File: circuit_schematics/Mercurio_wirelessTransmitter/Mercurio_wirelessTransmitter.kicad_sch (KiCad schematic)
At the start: 61 parts, among them J1 USB_B, J2 SIM_CARD_SLOT, J3 MAIN_ANTENNA, J4 SENSOR_IN, J5 ICSP, Q1 CSD16301Q2, Q2 CSD16301Q2, Q3 S8050, Q4 S8050, U1 ATmega8U2-MU, U2 SIM7600E-H, U3 ADS1115IDGS, U4 BQ29707DSET, U5 MT3608, Y1 16MHz

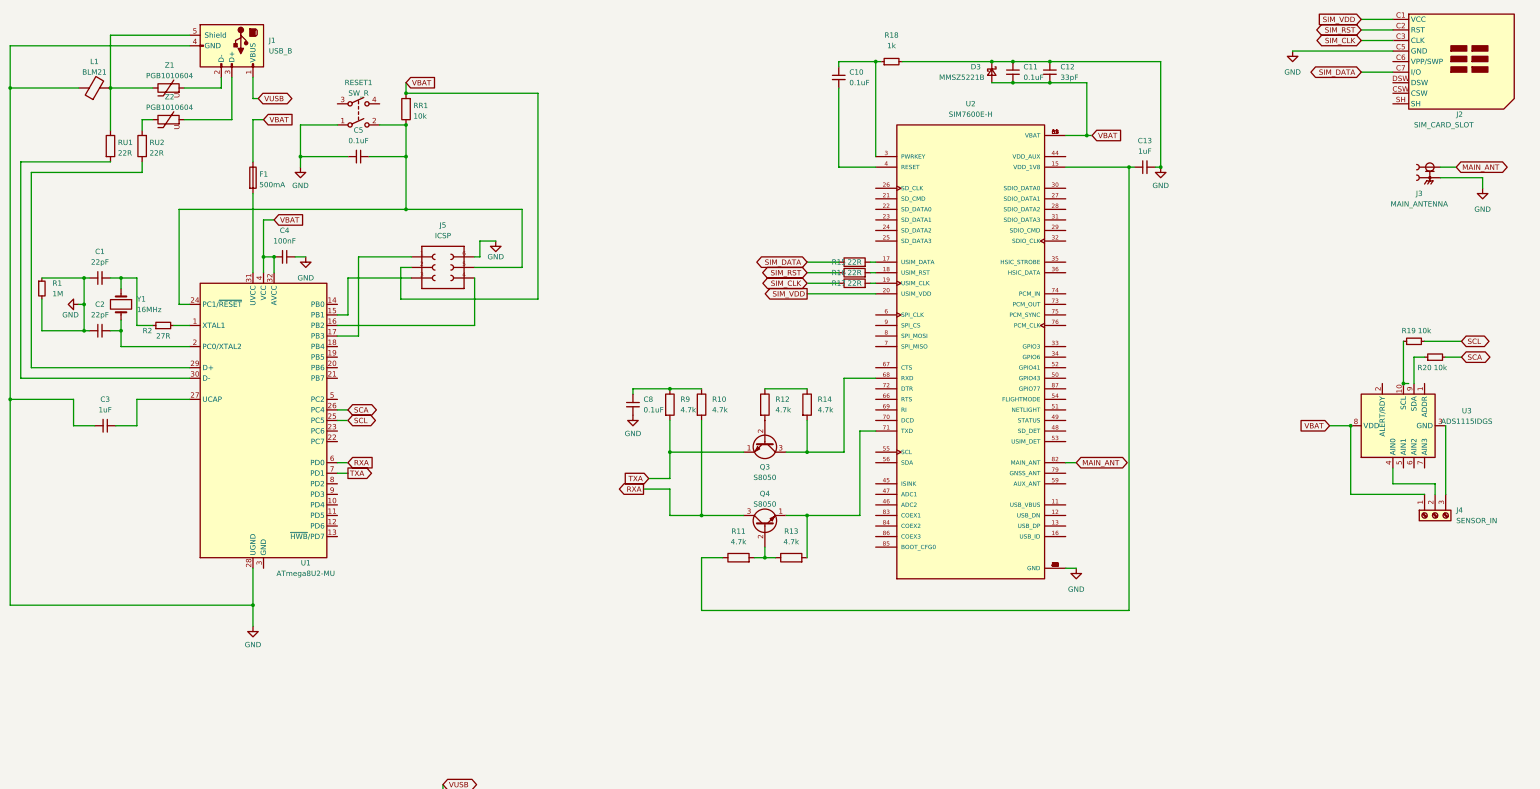
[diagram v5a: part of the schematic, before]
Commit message: Esquematico finalizado, PCB criada e organizada, lib atualizada.
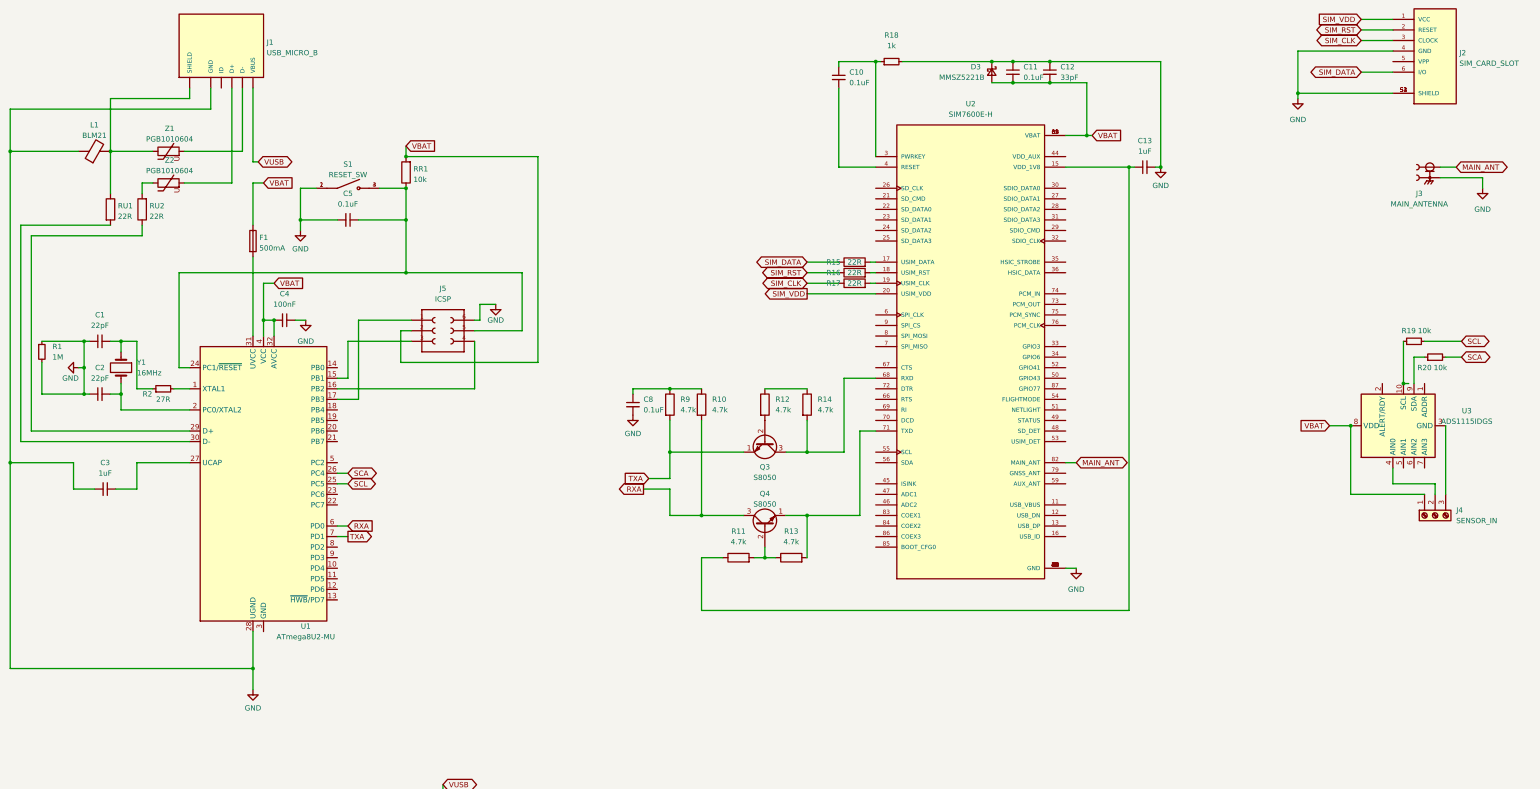
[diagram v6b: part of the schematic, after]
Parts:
- removed J1: USB_B, Connector_USB:USB_Micro-AB_Molex_47590-0001, symbol Connector:USB_B
- removed J2: SIM_CARD_SLOT, Connector_JAE:JAE_SIM_Card_SF72S006, symbol Connector:JAE_SIM_Card_SF72S006
- removed RESET1: SW_R, symbol Switch:SW_DPST
- added J1: USB_MICRO_B, USB3075-30-A:GCT_USB3075-30-A, symbol USB3075-30-A:USB3075-30-A
- added J2: SIM_CARD_SLOT, WURTH_693010020611, symbol 693010020611:693010020611
- added S1: RESET_SW, 5-1437565-0:SW_5-1437565-0, symbol 5-1437565-0:5-1437565-0
- L2: footprint (none) -> AIML-1206-120K-T:INDC3216X140N
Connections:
- net GND: now also J1.5 (GND), J2.4 (GND), J2.S1 (SHIELD), J2.S2 (SHIELD), J2.S3 (SHIELD), J2.S4 (SHIELD), S1.1, S1.2
- net SIM_CLK: now also J2.3 (CLOCK)
- net SIM_DATA: now also J2.6 (I/O)
- net SIM_RST: now also J2.2 (RESET)
- net SIM_VDD: now also J2.1 (VCC)
- net VUSB: now also J1.1 (VBUS)
- net at C5.1, J5.5, RR1.1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: now also S1.3, S1.4
- net at L1.2, RU1.1, Z1.1: now also J1.S1 (SHIELD), J1.S2 (SHIELD), J1.S3 (SHIELD), J1.S4 (SHIELD), J1.S5 (SHIELD), J1.S6 (SHIELD)
- net at Z1.2: now also J1.2 (D-)
- net at Z2.2: now also J1.3 (D+)
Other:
- moved on the sheet: C1, C2, C3, C4, C5, F1, J5, L1, R1, R2, RR1, RU1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
